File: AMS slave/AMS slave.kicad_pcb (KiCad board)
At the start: 2 copper layers, 68 x 95 mm, 109 parts, among them J1 Conn_02x08_Top_Bottom, J2 Conn_01x04, J3 Conn_02x03_Odd_Even, Q1 KY2N7002, Q2 AO3402, Q3 NCE60P04Y, SW1 SW_Push, SW2 SW_Push, U1 BQ76940DBT, U2 ATmega328P-A, U3 MCP2515-xST, U4 ISO1050DUB, Y1 20MHz, Y2 8MHz

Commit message: fixed VTAP collisions, AMS slave redesign WIP
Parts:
- removed NT1, NT2, NT3: NetTie_2, NetTie:NetTie-2_SMD_Pad0.5mm
- removed TH1, TH2, TH3, TH4, TH5: Conn_01x02_MountingPin, Connector_Molex:Molex_Micro-Fit_3.0_43650-0215_1x02_P3.00mm_Vertical
- added C31: 4.7uF, RMC_Capacitor:C_0805_2012Metric_Pad1.18x1.45mm_HandSolder_L, F.Cu at (-28.6, 67.0)
- added C32: 4.7uF, RMC_Capacitor:C_0805_2012Metric_Pad1.18x1.45mm_HandSolder_L, F.Cu at (-28.6, 70.0)
- added C35: 100nF, RMC_Capacitor:C_0805_2012Metric_Pad1.18x1.45mm_HandSolder_L, F.Cu at (-28.6, 73.0)
- added C36: 100nF, RMC_Capacitor:C_0805_2012Metric_Pad1.18x1.45mm_HandSolder_L, F.Cu at (-28.6, 76.1)
- added D5: 1N4148W, Diode_SMD:D_0805_2012Metric_Pad1.15x1.40mm_HandSolder, F.Cu at (-44.8, 93.4)
- added D6: 1N5822, Diode_THT:D_DO-201AD_P15.24mm_Horizontal, F.Cu at (-50.3, 77.6)
- added J4: Conn_01x05, Connector_Molex:Molex_Micro-Fit_3.0_43650-0415_1x04_P3.00mm_Vertical, F.Cu at (-7.50, 57.0)
- added R30: 10k, RMC_Resistor:R_0805_2012Metric_Pad1.20x1.40mm_HandSolder_L, F.Cu at (-9.15, 39.0)
- added R31: 120R, RMC_Resistor:R_0805_2012Metric_Pad1.20x1.40mm_HandSolder_L, F.Cu at (-28.7, 79.0)
- added R32: 10k, RMC_Resistor:R_0805_2012Metric_Pad1.20x1.40mm_HandSolder_L, F.Cu at (-50.0, 84.5)
- added R33: 10k, RMC_Resistor:R_0805_2012Metric_Pad1.20x1.40mm_HandSolder_L, F.Cu at (-50.0, 87.4)
- added R34: 10k, RMC_Resistor:R_0805_2012Metric_Pad1.20x1.40mm_HandSolder_L, F.Cu at (-50.0, 90.4)
- added R35: 10k, RMC_Resistor:R_0805_2012Metric_Pad1.20x1.40mm_HandSolder_L, F.Cu at (-50.0, 93.3)
- added R36: 10k, RMC_Resistor:R_0805_2012Metric_Pad1.20x1.40mm_HandSolder_L, F.Cu at (-50.0, 96.3)
- added U5: B0505S-2WR3, B0505S-2W3R:B_S-2WR2_MNS, F.Cu at (1.86, 116.6)
- added U6: LM2576HVS-3.3, Package_TO_SOT_SMD:TO-263-5_TabPin3, F.Cu at (-14.1, 75.0)
- C1, C10, C11, C13, C15, C16, C17, C20, C21, C22, C23, C24, C26, C27, C28, C29, C3, C30, C5, C6, C8, CAP1, CAP2, CAP3, Cf1, Cf2, Cf3, D1, D2, D3, D4, R12, R14, R15, R16, R2, R22, R27, R4, R7, R9, Rf1, Rf2, Rf3, Rx2, Rx3: moved to F.Cu
- C18, C19: value 22pF -> 12pF; moved to F.Cu
- J1: value Conn_02x08_Top_Bottom -> 559010274; footprint Connector_Molex:Molex_Micro-Fit_3.0_43045-1612_2x08_P3.00mm_Vertical -> CON_550910274_MOL:CON_550910274_MOL; moved to B.Cu
- J2: value Conn_01x04 -> Conn_02x03_Odd_Even; footprint Connector_JST:JST_XH_B4B-XH-A_1x04_P2.50mm_Vertical -> Connector_PinHeader_2.54mm:PinHeader_2x03_P2.54mm_Vertical
- J3: value Conn_02x03_Odd_Even -> Conn_01x05; footprint Connector_PinHeader_2.54mm:PinHeader_2x03_P2.54mm_Vertical -> Connector_Molex:Molex_Micro-Fit_3.0_43650-0415_1x04_P3.00mm_Vertical
- moved R14 195.3 mm to (-116.6, 61.3), turned to 0 degrees
- moved R13 192.6 mm to (-116.6, 58.4), turned to 0 degrees
- moved R12 190.1 mm to (-116.6, 55.4), turned to 0 degrees
- moved Q1 189.1 mm to (-122.2, 76.2)
- moved R11 187.7 mm to (-116.6, 52.5), turned to 0 degrees
- moved Q3 186.5 mm to (-115.0, 116.3), turned to 0 degrees
- moved Q2 184.4 mm to (-115.0, 111.8)
- moved R8 183.4 mm to (-122.1, 67.2), turned to 0 degrees
- moved R10 181.0 mm to (-116.6, 49.5), turned to 0 degrees
- moved R7 180.7 mm to (-122.1, 64.3), turned to 0 degrees
- moved Rx3 178.5 mm to (-111.2, 61.3), turned to 0 degrees
- moved R9 178.4 mm to (-116.6, 46.5), turned to 0 degrees
- moved R6 178.2 mm to (-122.1, 61.3), turned to 0 degrees
- moved C14 177.8 mm to (-100.2, 64.6)
- moved C13 175.3 mm to (-100.2, 61.6)
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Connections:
- net /cell monitoring/cell 9 renamed /cell monitoring/TP9
- C15 pad 2: +3V3 -> Net-(D5-A)
- C16 pad 2: +3V3 -> Net-(D5-A)
- J1 pad 1: GND -> PACK+
- J1 pad 10: /cell monitoring/cell 3 -> /NTC4+
- J1 pad 11: /cell monitoring/cell 5 -> /cell monitoring/TP13
- J1 pad 12: /cell monitoring/cell 7 -> /cell monitoring/TP11
- J1 pad 14: /cell monitoring/cell 11 -> /cell monitoring/TP7
- J1 pad 15: /cell monitoring/cell 13 -> /cell monitoring/TP5
- J1 pad 16: PACK+ -> /cell monitoring/TP3
- J1 pad 2: /cell monitoring/cell 2 -> /cell monitoring/TP12
- J1 pad 3: /cell monitoring/cell 4 -> /cell monitoring/TP10
- J1 pad 4: /cell monitoring/cell 6 -> /cell monitoring/TP8
- J1 pad 5: /cell monitoring/cell 8 -> /cell monitoring/TP6
- J1 pad 6: /cell monitoring/cell 10 -> /cell monitoring/TP4
- J1 pad 7: /cell monitoring/cell 12 -> /cell monitoring/TP2
- J1 pad 8: unconnected-(J1-Pin_8-Pad8) -> GND
- J1 pad 9: /cell monitoring/cell 1 -> /NTC2+
- J2 pad 1: VCC2 -> /MISO
- J2 pad 2: /CANH -> +3V3
- J2 pad 3: /CANL -> /SCK
- J2 pad 4: GND2 -> /MOSI
- J3 pad 1: /MISO -> VCC2
- J3 pad 2: +3V3 -> /CANH
- J3 pad 3: /SCK -> /CANL
- J3 pad 4: /MOSI -> GND2
- R1 pad 2: /cell monitoring/cell 1 -> /cell monitoring/TP1
- R10 pad 2: /cell monitoring/cell 10 -> /cell monitoring/TP10
- R11 pad 2: /cell monitoring/cell 11 -> /cell monitoring/TP11
- R12 pad 2: /cell monitoring/cell 12 -> /cell monitoring/TP12
- R13 pad 2: /cell monitoring/cell 13 -> /cell monitoring/TP13
- R2 pad 2: /cell monitoring/cell 2 -> /cell monitoring/TP2
- R28 pad 1: +3V3 -> Net-(U1-TS3)
- R28 pad 2: /TS4+ -> /cell monitoring/VC10X
- R29 pad 1: +3V3 -> Net-(U1-TS2)
- R29 pad 2: /TS5+ -> /cell monitoring/VC5X
- R3 pad 2: /cell monitoring/cell 3 -> /cell monitoring/TP3
- R4 pad 2: /cell monitoring/cell 4 -> /cell monitoring/TP4
- R5 pad 2: /cell monitoring/cell 5 -> /cell monitoring/TP5
- R6 pad 2: /cell monitoring/cell 6 -> /cell monitoring/TP6
- R7 pad 2: /cell monitoring/cell 7 -> /cell monitoring/TP7
- R8 pad 2: /cell monitoring/cell 8 -> /cell monitoring/TP8
- RBOOT1 pad 2: /cell monitoring/TS1+ -> /BQ_BOOT
- Rf1 pad 1: /cell monitoring/cell 5 -> /cell monitoring/TP5
- Rf2 pad 1: /cell monitoring/cell 10 -> /cell monitoring/TP10
- Rx2 pad 2: /cell monitoring/cell 5 -> /cell monitoring/TP5
- Rx3 pad 2: /cell monitoring/cell 10 -> /cell monitoring/TP10
- U1 pad 13: /cell monitoring/TS2+ -> Net-(U1-TS2)
- U1 pad 18: /cell monitoring/TS3+ -> Net-(U1-TS3)
- U1 pad 6: /cell monitoring/TS1+ -> /BQ_BOOT
- U1 pad 8: +3V3 -> Net-(D5-A)
- U2 pad 13: unconnected-(U2-PB1-Pad13) -> /STACK_READ
- U2 pad 19: unconnected-(U2-ADC6-Pad19) -> /STACK_VALUE
- U2 pad 22: unconnected-(U2-ADC7-Pad22) -> /NTC1+
- U2 pad 23: /STACK_VALUE -> /NTC2+
- U2 pad 24: /STACK_READ -> /NTC3+
- U2 pad 25: /TS5+ -> /NTC4+
- U2 pad 26: /TS4+ -> /NTC5+
- U2 pad 30: unconnected-(U2-PD0-Pad30) -> /BQ_BOOT
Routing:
- net GND: track 194.5 -> 0.00 mm, vias 35 -> 0
- net +3V3: track 155.3 -> 0.00 mm, vias 8 -> 0
- net /cell monitoring/cell 5: track 129.5 -> 0.00 mm
- net /cell monitoring/cell 10: track 114.2 -> 0.00 mm
- net PACK+: track 79.0 -> 0.00 mm, vias 1 -> 0
- net /TS5+: track 67.3 -> 0.00 mm, vias 2 -> 0
- net /TS4+: track 58.7 -> 0.00 mm, vias 2 -> 0
- net /cell monitoring/TS1+: track 50.0 -> 0.00 mm, vias 4 -> 0
- net /cell monitoring/TS1-: track 39.6 -> 0.00 mm
- net /STACK_VALUE: track 36.5 -> 0.00 mm, vias 2 -> 0
- net /cell monitoring/VC5X: track 35.8 -> 0.00 mm, vias 4 -> 0
- net /cell monitoring/TS3+: track 35.4 -> 0.00 mm, vias 2 -> 0
- net /cell monitoring/TS2+: track 35.0 -> 0.00 mm, vias 2 -> 0
- net Net-(U3-RXCAN): track 34.5 -> 0.00 mm, vias 2 -> 0
- net /STACK_READ: track 34.3 -> 0.00 mm, vias 2 -> 0
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- removed copper zone on B.Cu, net GND
- removed copper zone on F.Cu, net GND
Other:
- board size 68 x 95 mm -> 68 x 100 mm
- board text removed: "+"
- board text removed: "+3V3"
- board text removed: "-"
- board text removed: "1"
- board text removed: "10"
- board text removed: "11"
- board text removed: "12"
- board text removed: "13"
- board text removed: "2"
- board text removed: "3"
- board text removed: "4"
- board text removed: "5"
- board text removed: "6"
- board text removed: "7"
- board text removed: "8"
- board text removed: "9"
- board text removed: "CANH"
- board text removed: "CANL"
- board text removed: "GND"
- board text removed: "GND2"
- board text removed: "MISO"
- board text removed: "MOSI"
- board text removed: "NC"
- board text removed: "RST"
- board text removed: "SCK"
- board text removed: "VCC2"

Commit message: AMS slave WIP
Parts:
- added C33: 330uF, RMC_Capacitor:CP_Radial_D6.3mm_P2.50mm_handsolder, F.Cu at (38.9, 59.6)
- added C34: 330uF, RMC_Capacitor:CP_Radial_D6.3mm_P2.50mm_handsolder, F.Cu at (38.9, 69.2)
- added L1: 47uH, RMC_Inductor:L_10.4x10.4_H4.8_handsolder, F.Cu at (53.5, 60.9)
- C1, C10, C11, C13, C3, C5, C6, C8: moved to B.Cu
- moved R7 335.9 mm to (213.8, 58.9)
- moved R8 335.9 mm to (213.8, 61.9)
- moved R13 335.9 mm to (219.3, 58.9)
- moved R14 335.9 mm to (219.3, 61.9)
- moved R10 331.0 mm to (213.8, 67.8)
- moved R11 331.0 mm to (213.8, 70.7)
- moved R12 331.0 mm to (213.8, 73.7)
- moved R9 331.0 mm to (213.8, 64.8)
- moved R1 330.7 mm to (208.4, 58.9)
- moved R2 330.7 mm to (208.4, 61.9)
- moved R3 330.7 mm to (208.4, 64.8)
- moved R4 330.7 mm to (208.4, 67.8)
- moved R5 330.7 mm to (208.4, 70.7)
- moved R6 330.7 mm to (208.4, 73.7)
- moved Rx1 330.6 mm to (219.3, 64.8)
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
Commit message: AMS slave schem updated
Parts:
- C18, C19, C20, C21, C22, C23, C24, C28, C29, C31, C32, CAP1, CAP2, CAP3, Cf1, Cf2, Cf3, D1, D2, R1, R10, R11, R13, R16, R27, R28, R29, R3, R30, R5, R6, R8, Rf1, Rf2, Rf3: moved to B.Cu
- C33: value 330uF -> 110uF
- D5: value 1N4148W -> BAT85; footprint Diode_SMD:D_0805_2012Metric_Pad1.15x1.40mm_HandSolder -> Diode_THT:D_DO-35_SOD27_P7.62mm_Horizontal
- moved RBOOT1 269.4 mm to (152.1, 86.8)
- moved SW1 265.0 mm to (145.0, 86.8)
- moved C16 264.7 mm to (169.5, 64.2)
- moved C17 264.7 mm to (169.5, 67.2)
- moved C25 264.7 mm to (147.7, 103.2)
- moved C26 264.7 mm to (147.7, 106.3)
- moved C27 264.7 mm to (147.7, 109.3)
- moved C30 264.7 mm to (153.2, 103.2)
- moved JP1 264.7 mm to (174.4, 97.5)
- moved JP2 264.7 mm to (174.4, 101.0)
- moved JP3 264.7 mm to (174.4, 104.6)
- moved JP4 264.7 mm to (174.4, 108.2)
- moved R17 264.7 mm to (158.6, 100.2)
- moved R18 264.7 mm to (158.6, 103.1)
- moved R19 264.7 mm to (158.6, 106.1)
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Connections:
- C15 pad 2: Net-(D5-A) -> +3V3
- R33 pad 1: /NTC2+ -> +3V3
- R33 pad 2: +3V3 -> /NTC2+
- R35 pad 1: /NTC4+ -> +3V3
- R35 pad 2: +3V3 -> /NTC4+
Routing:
- net GND: track 0.00 -> 69.0 mm, vias 0 -> 2
- net +3V3: track 0.00 -> 60.2 mm, vias 0 -> 4
- net /cell monitoring/TP5: track 0.00 -> 46.6 mm, vias 0 -> 1
- net /cell monitoring/VC15: track 0.00 -> 34.3 mm, vias 0 -> 1
- net /cell monitoring/VC0: track 0.00 -> 34.0 mm, vias 0 -> 1
- net PACK+: track 0.00 -> 32.2 mm, vias 0 -> 1
- net /cell monitoring/VC10X: track 0.00 -> 30.8 mm, vias 0 -> 2
- net /cell monitoring/VC13: track 0.00 -> 30.1 mm, vias 0 -> 1
- net /cell monitoring/VC1: track 0.00 -> 29.6 mm, vias 0 -> 1
- net /cell monitoring/VC12: track 0.00 -> 27.7 mm, vias 0 -> 1
- net /cell monitoring/VC2: track 0.00 -> 27.7 mm, vias 0 -> 1
- net /cell monitoring/VC5X: track 0.00 -> 26.7 mm, vias 0 -> 2
- net /cell monitoring/VC3: track 0.00 -> 25.7 mm, vias 0 -> 1
- net /cell monitoring/VC11: track 0.00 -> 25.7 mm, vias 0 -> 1
- net /cell monitoring/TP12: track 0.00 -> 24.8 mm, vias 0 -> 1
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
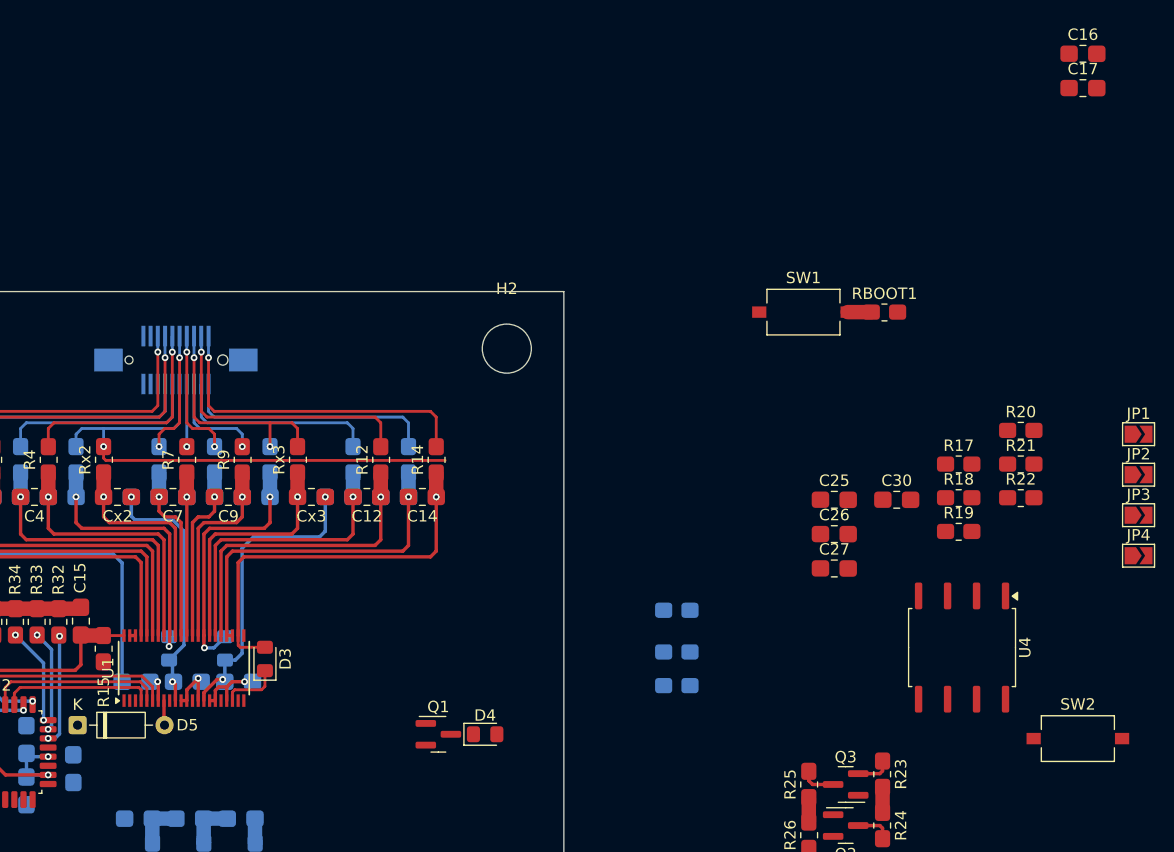
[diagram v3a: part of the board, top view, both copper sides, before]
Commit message: fixed TS/LVS separation requirements
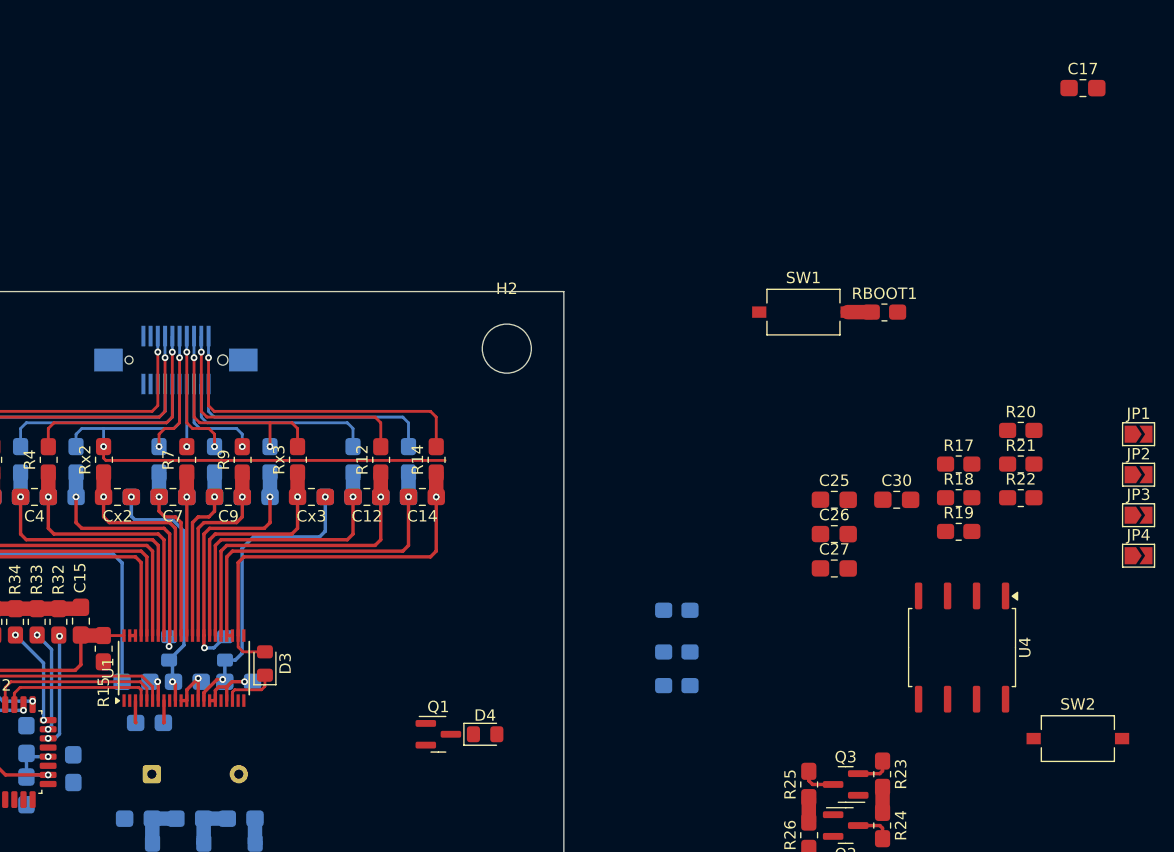
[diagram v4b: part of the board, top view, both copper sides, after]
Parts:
- C16, D5: moved to B.Cu
- moved C16 100.7 mm to (87.7, 122.8)
- moved D5 7.80 mm to (87.9, 127.3)
- moved D3 0.40 mm to (97.8, 117.6)
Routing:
- net GND: track 69.0 -> 71.0 mm
